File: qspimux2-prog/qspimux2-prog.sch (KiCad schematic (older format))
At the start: 14 parts, among them J101 Conn_02x03_Odd_Even, U101 STM32F042C6Tx

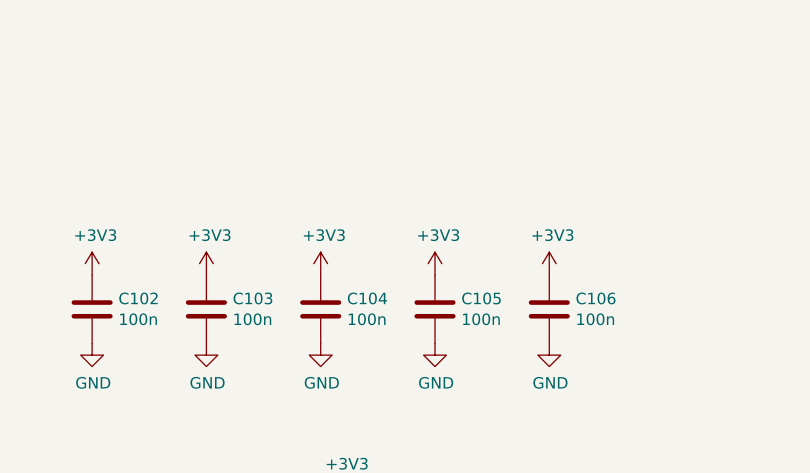
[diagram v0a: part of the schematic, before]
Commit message: add a few missing capacitors and do some slight layout optimizations
add two missing capacitors on the supply rails of the microcontroller
add capacitor to vtarget monitoringto get a low pass
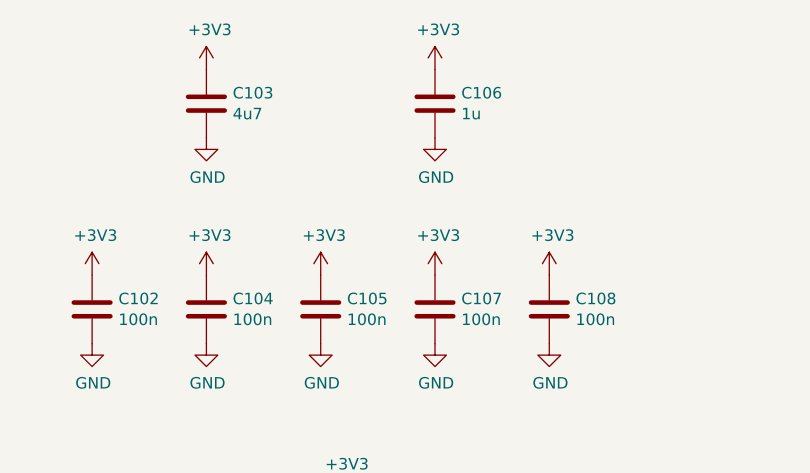
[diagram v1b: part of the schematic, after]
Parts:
- added C103: 4u7, Capacitor_SMD:C_0603_1608Metric, symbol Device:C
- added C106: 1u, Capacitor_SMD:C_0603_1608Metric, symbol Device:C
- renumbered C103 to C104, C104 to C105, C105 to C107, C106 to C108
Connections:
- net +3V3: now also C103.1, C106.1
- net GND: now also C103.2, C106.2
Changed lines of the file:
@@
 	5100 3100 5100 3200
 $Comp
-L power:+3V3 #PWR0113
+L power:+3V3 #PWR0115
 U 1 1 5E0BEA36
 P 5100 3100
-F 0 "#PWR0113" H 5100 2950 50  0001 C CNN
+F 0 "#PWR0115" H 5100 2950 50  0001 C CNN
 F 1 "+3V3" H 5115 3273 50  0000 C CNN
 F 2 "" H 5100 3100 50  0001 C CNN
@@
 $EndComp
 $Comp
-L Device:C C103
+L Device:C C104
 U 1 1 5E2E1550
 P 4500 2250
-F 0 "C103" H 4615 2296 50  0000 L CNN
+F 0 "C104" H 4615 2296 50  0000 L CNN
 F 1 "100n" H 4615 2205 50  0000 L CNN
 F 2 "Capacitor_SMD:C_0402_1005Metric" H 4538 2100 50  0001 C CNN
@@
 $EndComp
 $Comp
-L power:GND #PWR0109
+L power:GND #PWR0111
 U 1 1 5E2E155D
 P 4500 2400
-F 0 "#PWR0109" H 4500 2150 50  0001 C CNN
+F 0 "#PWR0111" H 4500 2150 50  0001 C CNN
 F 1 "GND" H 4505 2227 50  0000 C CNN
 F 2 "" H 4500 2400 50  0001 C CNN
@@
 $EndComp
 $Comp
-L Device:C C104
+L Device:C C105
 U 1 1 5E2E156B
 P 5000 2250
-F 0 "C104" H 5115 2296 50  0000 L CNN
+F 0 "C105" H 5115 2296 50  0000 L CNN
 F 1 "100n" H 5115 2205 50  0000 L CNN
 F 2 "Capacitor_SMD:C_0402_1005Metric" H 5038 2100 50  0001 C CNN
@@
 $EndComp
 $Comp
-L power:+3V3 #PWR0110
+L power:+3V3 #PWR0112
 U 1 1 5E2E1578
 P 5000 2100
-F 0 "#PWR0110" H 5000 1950 50  0001 C CNN
+F 0 "#PWR0112" H 5000 1950 50  0001 C CNN
 F 1 "+3V3" H 5015 2273 50  0000 C CNN
 F 2 "" H 5000 2100 50  0001 C CNN
@@
 $EndComp
 $Comp
-L power:GND #PWR0111
+L power:GND #PWR0113
 U 1 1 5E2E1585
 P 5000 2400
-F 0 "#PWR0111" H 5000 2150 50  0001 C CNN
+F 0 "#PWR0113" H 5000 2150 50  0001 C CNN
 F 1 "GND" H 5005 2227 50  0000 C CNN
 F 2 "" H 5000 2400 50  0001 C CNN
@@
 $EndComp
 $Comp
-L power:+3V3 #PWR0108
+L power:+3V3 #PWR0110
 U 1 1 5E2E1592
 P 4500 2100
-F 0 "#PWR0108" H 4500 1950 50  0001 C CNN
+F 0 "#PWR0110" H 4500 1950 50  0001 C CNN
 F 1 "+3V3" H 4515 2273 50  0000 C CNN
 F 2 "" H 4500 2100 50  0001 C CNN
@@
 Connection ~ 5000 3200
 $Comp
-L Device:C C105
+L Device:C C107
 U 1 1 5DF4A9B7
 P 5500 2250
-F 0 "C105" H 5615 2296 50  0000 L CNN
+F 0 "C107" H 5615 2296 50  0000 L CNN
 F 1 "100n" H 5615 2205 50  0000 L CNN
 F 2 "Capacitor_SMD:C_0402_1005Metric" H 5538 2100 50  0001 C CNN
@@
 $EndComp
 $Comp
-L power:GND #PWR0115
+L power:GND #PWR0119
 U 1 1 5DF4A9C4
 P 5500 2400
-F 0 "#PWR0115" H 5500 2150 50  0001 C CNN
+F 0 "#PWR0119" H 5500 2150 50  0001 C CNN
 F 1 "GND" H 5505 2227 50  0000 C CNN
 F 2 "" H 5500 2400 50  0001 C CNN
@@
 $EndComp
 $Comp
-L Device:C C106
+L Device:C C108
 U 1 1 5DF4A9D2
 P 6000 2250
-F 0 "C106" H 6115 2296 50  0000 L CNN
+F 0 "C108" H 6115 2296 50  0000 L CNN
 F 1 "100n" H 6115 2205 50  0000 L CNN
 F 2 "Capacitor_SMD:C_0402_1005Metric" H 6038 2100 50  0001 C CNN
@@
 $EndComp
 $Comp
-L power:+3V3 #PWR0116
+L power:+3V3 #PWR0120
 U 1 1 5DF4A9DF
 P 6000 2100
-F 0 "#PWR0116" H 6000 1950 50  0001 C CNN
+F 0 "#PWR0120" H 6000 1950 50  0001 C CNN
 F 1 "+3V3" H 6015 2273 50  0000 C CNN
 F 2 "" H 6000 2100 50  0001 C CNN
@@
 $EndComp
 $Comp
-L power:GND #PWR0117
+L power:GND #PWR0121
 U 1 1 5DF4A9EC
 P 6000 2400
-F 0 "#PWR0117" H 6000 2150 50  0001 C CNN
+F 0 "#PWR0121" H 6000 2150 50  0001 C CNN
 F 1 "GND" H 6005 2227 50  0000 C CNN
 F 2 "" H 6000 2400 50  0001 C CNN
@@
 $EndComp
 $Comp
-L power:+3V3 #PWR0114
+L power:+3V3 #PWR0118
 U 1 1 5DF4A9F9
 P 5500 2100
-F 0 "#PWR0114" H 5500 1950 50  0001 C CNN
+F 0 "#PWR0118" H 5500 1950 50  0001 C CNN
 F 1 "+3V3" H 5515 2273 50  0000 C CNN
 F 2 "" H 5500 2100 50  0001 C CNN
@@
 $EndComp
 $Comp
-L power:GND #PWR0112
+L power:GND #PWR0114
 U 1 1 5DFA78DD
 P 5000 6400
-F 0 "#PWR0112" H 5000 6150 50  0001 C CNN
+F 0 "#PWR0114" H 5000 6150 50  0001 C CNN
 F 1 "GND" H 5005 6227 50  0000 C CNN
 F 2 "" H 5000 6400 50  0001 C CNN
@@
 	1    0    0    -1
 $EndComp
+$Comp
+L Device:C C106
+U 1 1 5DFACDE5
+P 5500 1350
+F 0 "C106" H 5615 1396 50  0000 L CNN
+F 1 "1u" H 5615 1305 50  0000 L CNN
+F 2 "Capacitor_SMD:C_0603_1608Metric" H 5538 1200 50  0001 C CNN
+F 3 "~" H 5500 1350 50  0001 C CNN
+	1    5500 1350
+	1    0    0    -1
+$EndComp
+$Comp
+L power:GND #PWR0117
+U 1 1 5DFAE113
+P 5500 1500
+F 0 "#PWR0117" H 5500 1250 50  0001 C CNN
+F 1 "GND" H 5505 1327 50  0000 C CNN
+F 2 "" H 5500 1500 50  0001 C CNN
+F 3 "" H 5500 1500 50  0001 C CNN
+	1    5500 1500
+	1    0    0    -1
+$EndComp
+$Comp
+L power:+3V3 #PWR0116
+U 1 1 5DFB06CE
+P 5500 1200
+F 0 "#PWR0116" H 5500 1050 50  0001 C CNN
+F 1 "+3V3" H 5515 1373 50  0000 C CNN
+F 2 "" H 5500 1200 50  0001 C CNN
+F 3 "" H 5500 1200 50  0001 C CNN
+	1    5500 1200
+	1    0    0    -1
+$EndComp
+$Comp
+L power:+3V3 #PWR0108
+U 1 1 5E04B281
+P 4500 1200
+F 0 "#PWR0108" H 4500 1050 50  0001 C CNN
+F 1 "+3V3" H 4515 1373 50  0000 C CNN
+F 2 "" H 4500 1200 50  0001 C CNN
+F 3 "" H 4500 1200 50  0001 C CNN
+	1    4500 1200
+	1    0    0    -1
+$EndComp
+$Comp
+L power:GND #PWR0109
+U 1 1 5E04B28E
+P 4500 1500
+F 0 "#PWR0109" H 4500 1250 50  0001 C CNN
+F 1 "GND" H 4505 1327 50  0000 C CNN
+F 2 "" H 4500 1500 50  0001 C CNN
+F 3 "" H 4500 1500 50  0001 C CNN
+	1    4500 1500
+	1    0    0    -1
+$EndComp
+$Comp
+L Device:C C103
+U 1 1 5E04B29C
+P 4500 1350
+F 0 "C103" H 4615 1396 50  0000 L CNN
+F 1 "4u7" H 4615 1305 50  0000 L CNN
+F 2 "Capacitor_SMD:C_0603_1608Metric" H 4538 1200 50  0001 C CNN
+F 3 "~" H 4500 1350 50  0001 C CNN
+	1    4500 1350
+	1    0    0    -1
+$EndComp
